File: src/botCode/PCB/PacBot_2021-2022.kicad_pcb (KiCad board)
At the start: 2 copper layers, 24 parts, among them J1 conn_imu, J2 conn_motor-encoder_L, J3 conn_motor-encoder_R, J4 RPi_GPIO, J5 Conn_Batt, U1 L7805, U2 Teensy-LC, U3 VL6180X, U4 DRV8835, U5 VL6180X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

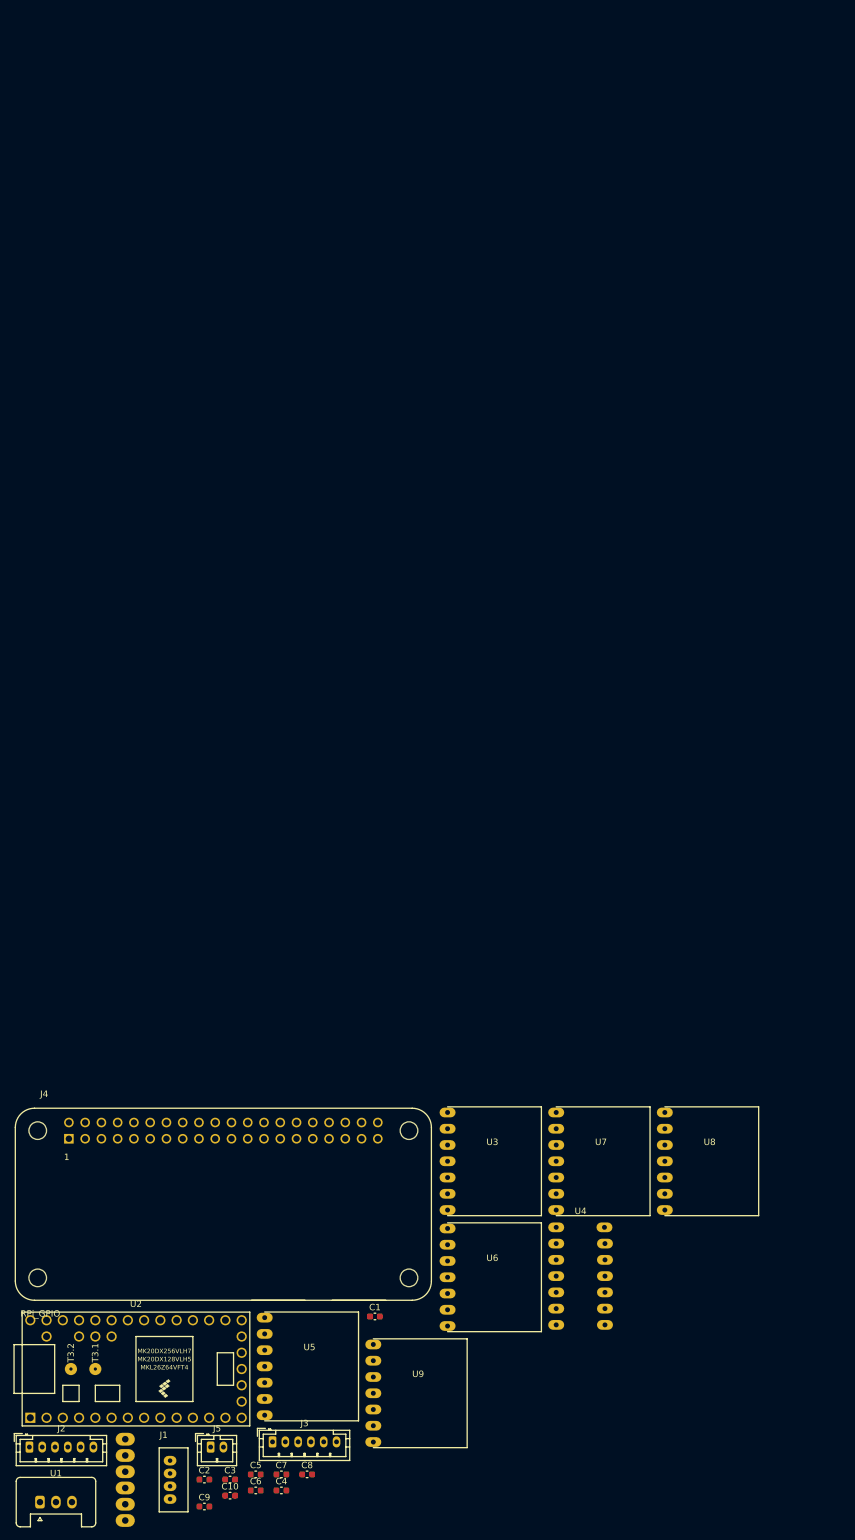
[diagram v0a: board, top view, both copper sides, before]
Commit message: added board outline
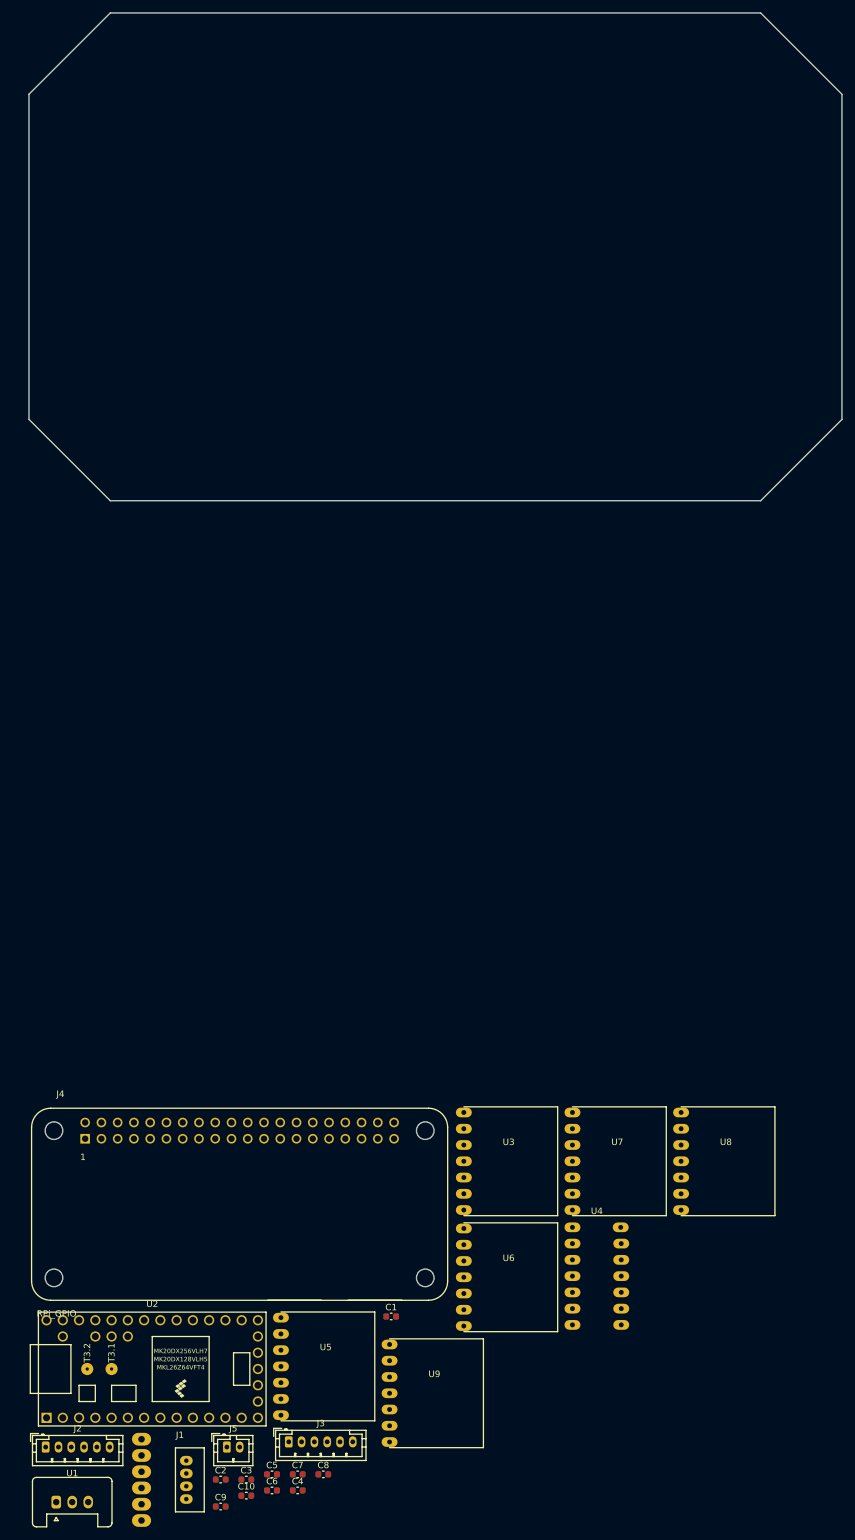
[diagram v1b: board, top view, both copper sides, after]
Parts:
- moved C1 2.54 mm to (149.9, 106.7)
- moved C5 2.54 mm to (131.2, 131.3)
- moved C6 2.54 mm to (131.2, 133.9)
- moved J3 2.54 mm to (133.9, 126.3)
- moved U3 2.54 mm to (161.2, 82.4)
- moved U4 2.54 mm to (182.0, 100.4)
- moved U6 2.54 mm to (161.2, 100.6)
- moved U7 2.54 mm to (178.2, 82.4)
- moved U8 2.54 mm to (195.1, 82.4)
- moved C10 2.54 mm to (127.2, 134.7)
- moved C3 2.54 mm to (127.2, 132.2)
- moved J1 2.54 mm to (110.9, 132.2)
- moved J4 2.54 mm to (126.2, 77.7)
- moved U1 2.54 mm to (97.5, 135.7)
- moved U2 2.54 mm to (112.5, 114.9)
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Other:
- board outline added: 127 x 76.2 mm

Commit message: added the vias and guiding labels
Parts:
- moved U9 219.7 mm to (363.8, 69.6)
- moved C1 219.7 mm to (364.0, 57.6)
- moved C10 219.7 mm to (341.4, 85.6)
- moved C3 219.7 mm to (341.4, 83.1)
- moved C4 219.7 mm to (349.4, 84.8)
- moved C5 219.7 mm to (345.4, 82.3)
- moved C6 219.7 mm to (345.4, 84.8)
- moved C7 219.7 mm to (349.4, 82.3)
- moved C8 219.7 mm to (353.4, 82.3)
- moved J1 219.7 mm to (325.0, 83.1)
- moved J2 219.7 mm to (310.1, 78.0)
- moved J3 219.7 mm to (348.0, 77.2)
- moved J4 219.7 mm to (340.4, 28.6)
- moved J5 219.7 mm to (338.4, 78.0)
- moved U4 219.7 mm to (396.2, 51.3)
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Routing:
- net (no net): vias 0 -> 16

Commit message: added some components + adjusted Pi position
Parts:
- moved U4 274.4 mm to (127.1, 105.0)
- moved J4 236.5 mm to (116.6, 105.0), turned to -90 degrees
- moved J3 227.4 mm to (127.1, 131.0), turned to 90 degrees
- moved J2 183.3 mm to (127.1, 89.0), turned to 90 degrees
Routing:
- net Net-(J2-Pad6): vias 0 -> 1
- net (no net): vias 16 -> 11

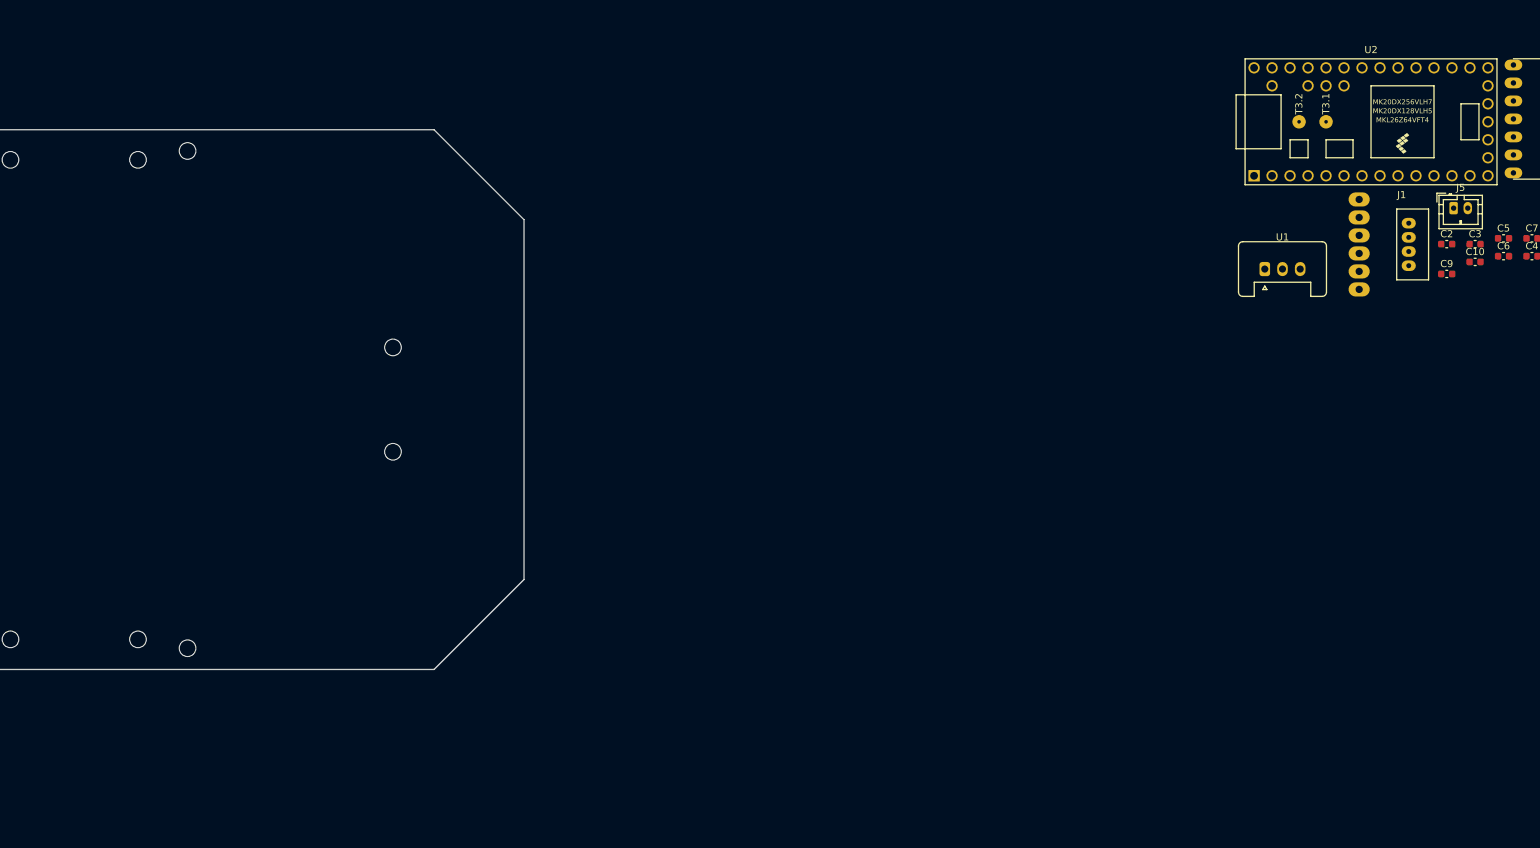
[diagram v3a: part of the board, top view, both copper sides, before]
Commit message: Added Teensy, holes need to be moved
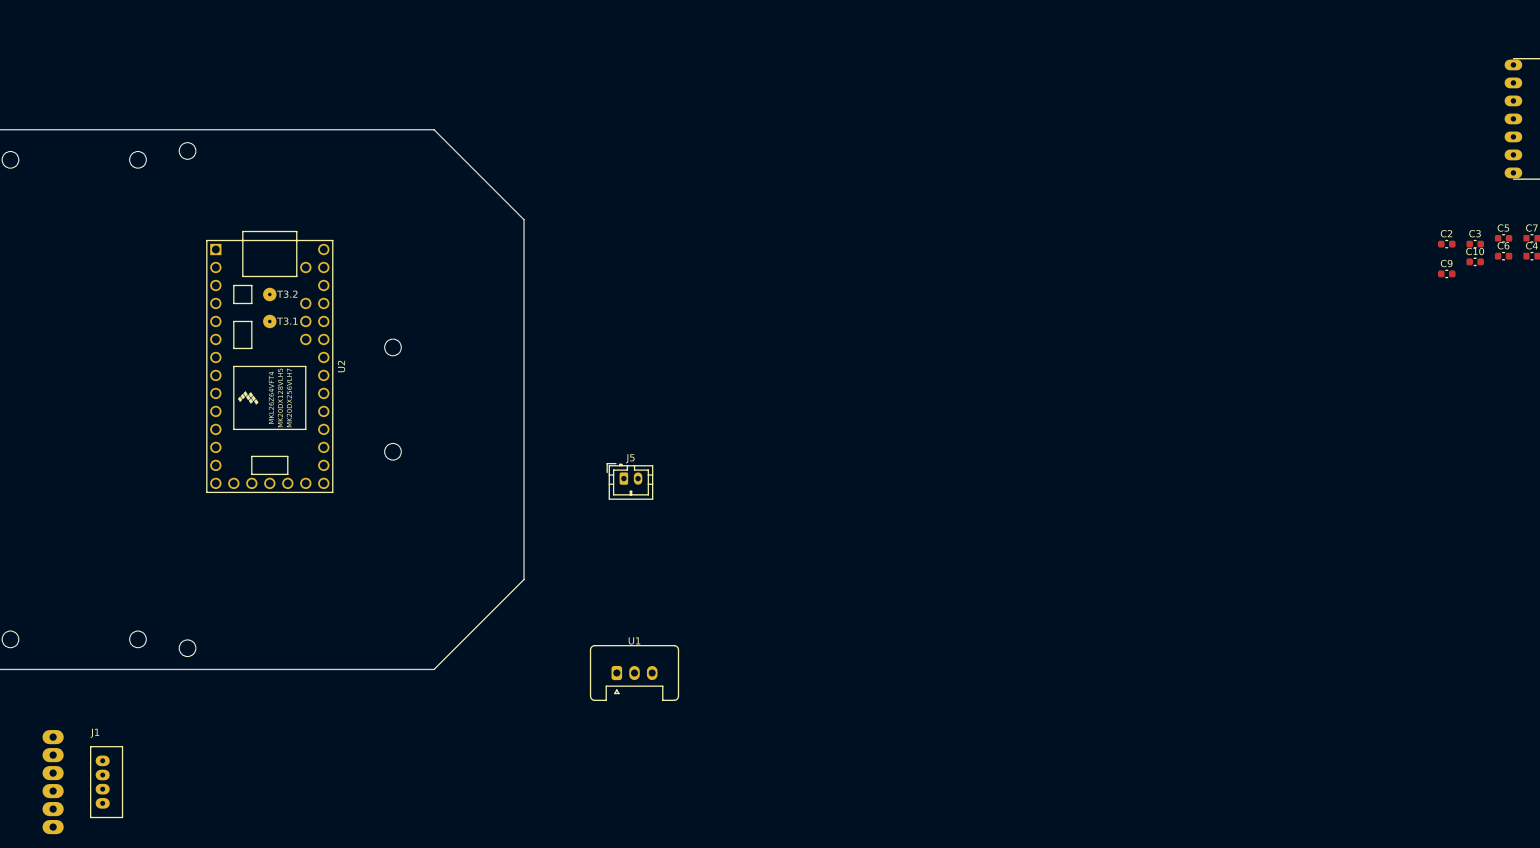
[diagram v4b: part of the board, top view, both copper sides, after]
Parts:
- moved J1 199.4 mm to (140.7, 159.0)
- moved U2 159.3 mm to (171.2, 100.3), turned to -90 degrees
- moved J5 123.2 mm to (221.2, 116.2)
- moved U1 107.8 mm to (220.2, 143.6)

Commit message: Holes moved, some more components added
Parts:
- moved U6 206.9 mm to (183.2, 128.1), turned to -90 degrees
- moved U3 196.8 mm to (192.1, 105.0)
- moved U5 164.4 mm to (183.2, 81.9), turned to 90 degrees
- moved C9 142.8 mm to (195.3, 101.3), turned to -90 degrees
- moved J5 53.3 mm to (169.6, 129.6), turned to -90 degrees
- moved U1 28.4 mm to (232.8, 118.1)
- moved U2 3.16 mm to (172.2, 103.3)
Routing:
- net /SDA0: vias 0 -> 1
- net (no net): vias 11 -> 10

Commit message: some PCB updates
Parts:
- C1, C10, C2, C3, C4, C6, C7, C9: moved to B.Cu
- moved U8 322.3 mm to (95.1, 105.0), turned to 180 degrees
- moved U7 292.4 mm to (104.0, 81.9), turned to 90 degrees
- moved C1 266.9 mm to (107.6, 131.7), turned to 180 degrees
- moved U9 266.3 mm to (104.0, 128.1), turned to -90 degrees
- moved C6 254.3 mm to (92.3, 108.9), turned to 90 degrees
- moved C4 249.2 mm to (100.3, 78.8)
- moved C5 233.8 mm to (111.6, 86.2), turned to -90 degrees
- moved C7 222.9 mm to (127.1, 98.7), turned to 90 degrees
- moved C8 215.3 mm to (140.9, 116.8)
- moved C3 161.9 mm to (179.5, 78.8), turned to 180 degrees
- moved C10 161.0 mm to (187.1, 131.6), turned to 180 degrees
- moved C2 154.7 mm to (182.8, 88.2), turned to -90 degrees
- moved U1 73.2 mm to (161.2, 133.0), turned to 90 degrees
- moved J1 54.0 mm to (135.3, 105.3)
- moved C9 0.32 mm to (195.7, 101.3)
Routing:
- net unconnected-(U8-Pad1): vias 0 -> 1
- net /IRE_EN: vias 0 -> 1
- net (no net): vias 10 -> 8

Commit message: PCB updated
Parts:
- C2: moved to F.Cu
- C5, C8: moved to B.Cu
- moved C2 45.0 mm to (164.1, 129.1)
- moved C8 15.3 mm to (138.7, 101.8), turned to -90 degrees
- moved C5 1.53 mm to (112.3, 87.6)

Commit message: PCB components placed
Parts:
- moved U1 12.9 mm to (172.6, 127.0), turned to 180 degrees
- moved C2 6.82 mm to (168.7, 124.1), turned to 0 degrees
- moved J5 5.54 mm to (170.6, 135.1), turned to 180 degrees
- moved C10 2.30 mm to (189.4, 131.6)
- moved C3 2.30 mm to (181.8, 78.8)
- moved C1 2.30 mm to (105.3, 131.7)
- moved C4 2.30 mm to (98.0, 78.8)
- moved U7 2.30 mm to (101.7, 81.9)
- moved U9 2.30 mm to (101.7, 128.1)
- moved U6 2.30 mm to (185.5, 128.1)
- moved U5 2.29 mm to (185.5, 81.9)
- moved U2 2.19 mm to (170.1, 103.3), turned to 90 degrees
- moved J1 0.68 mm to (134.7, 105.0)
- moved C8 0.60 mm to (138.1, 101.8)
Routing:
- net unconnected-(U2-Pad19): vias 0 -> 1
- net unconnected-(U2-Pad14): vias 0 -> 1
- net /SDA0: vias 1 -> 0
- net (no net): vias 8 -> 7
